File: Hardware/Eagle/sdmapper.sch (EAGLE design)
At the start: 27 parts, among them IC1 AM29F010J, IC2 HM628512ASOP32, IC3 XC95144XL_TQ100, IC4 LM1117-3V3, T1 BC558, T2 BC558

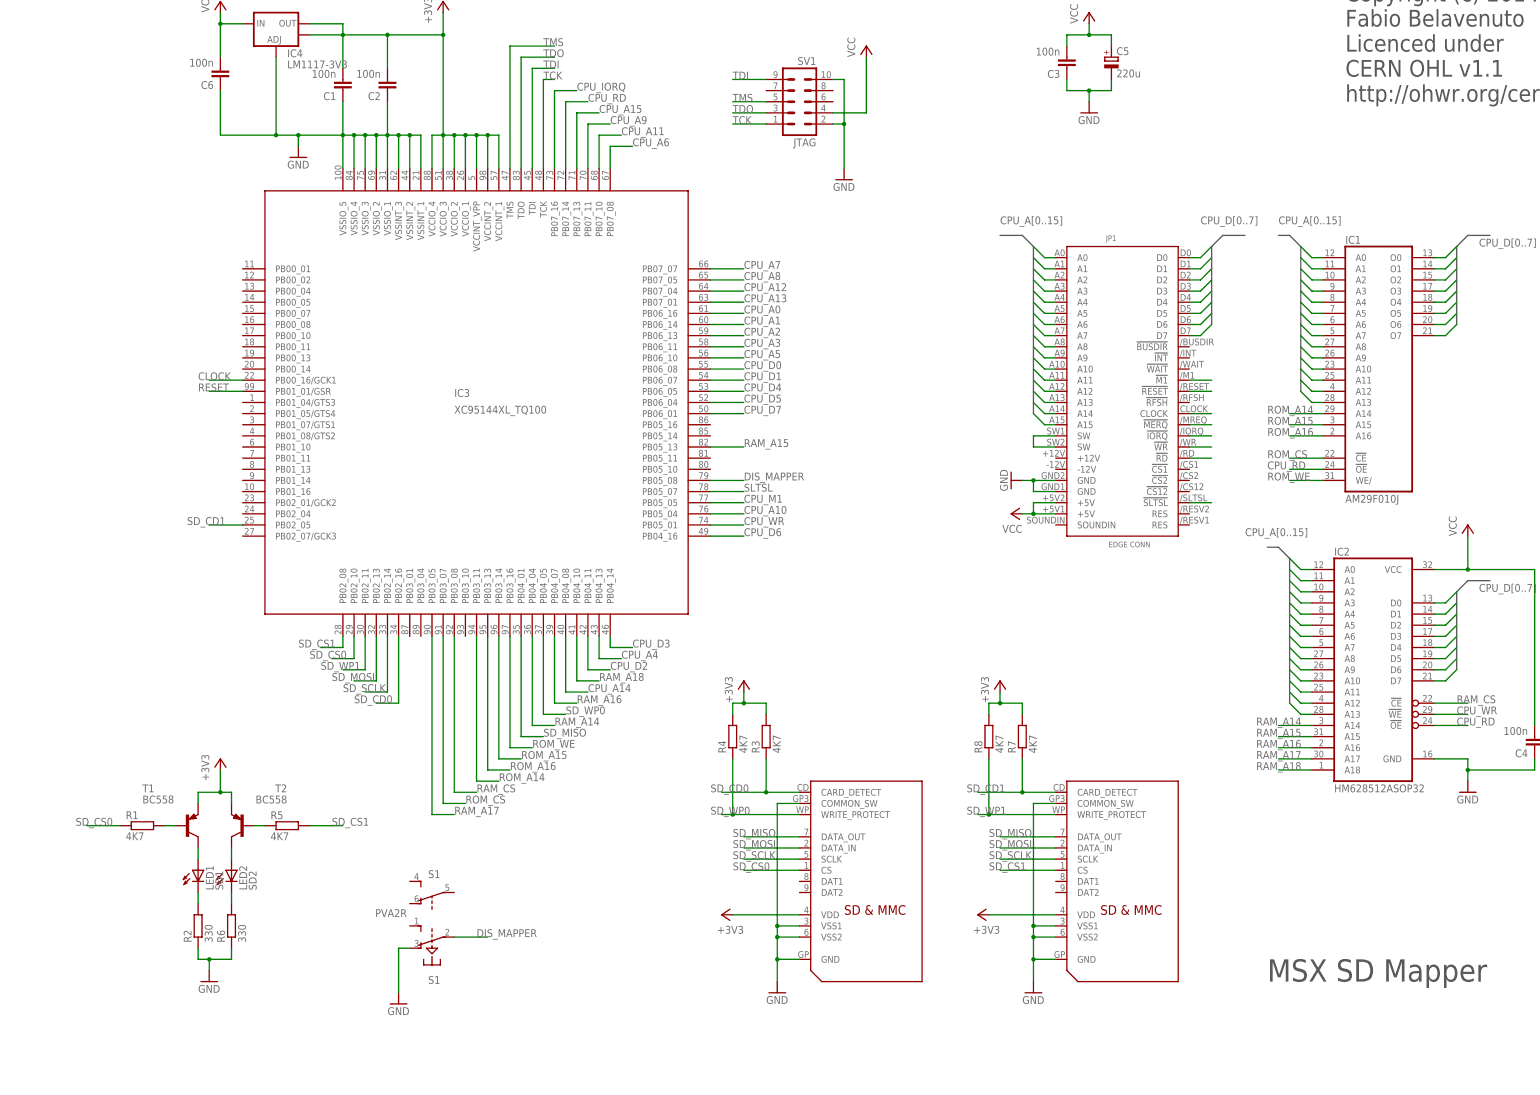
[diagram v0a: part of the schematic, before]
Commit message: Terminado layout da placa Atualizado esquema.pdf Atualizado pinout no projeto do ISE
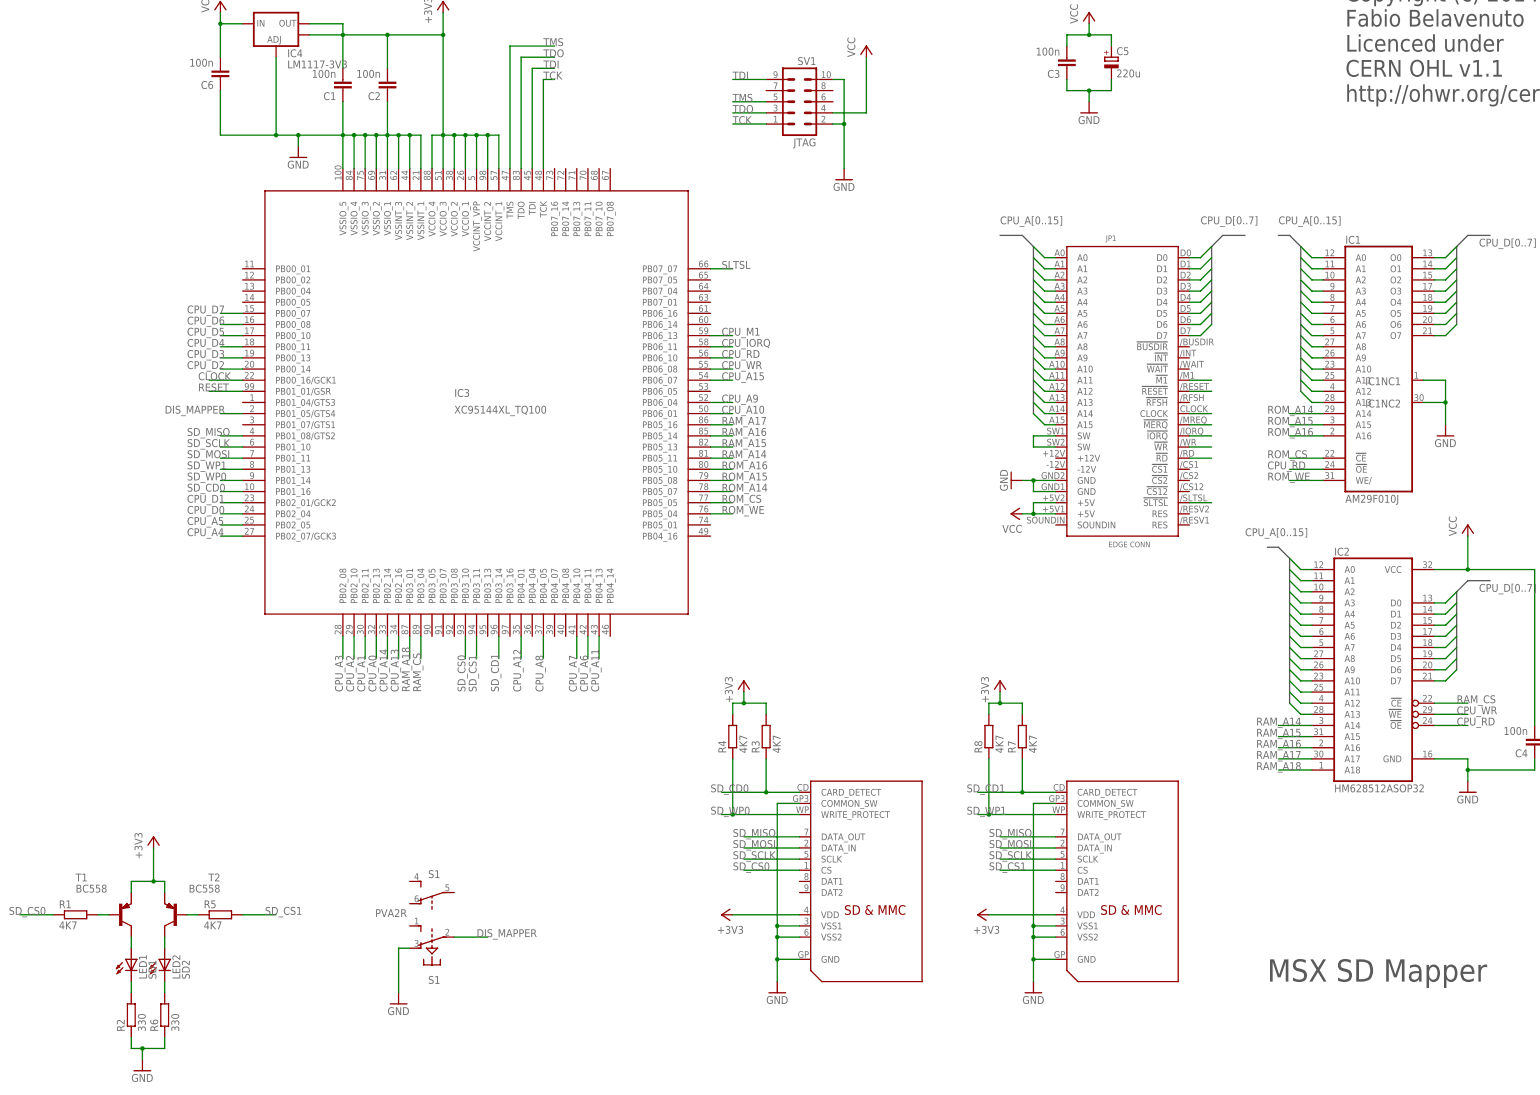
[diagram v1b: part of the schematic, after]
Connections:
- net CPU_A0: now also IC3.PB02_13; no longer IC3.PB06_16
- net CPU_A1: now also IC3.PB02_11; no longer IC3.PB06_14
- net CPU_A10: now also IC3.PB06_01; no longer IC3.PB05_04
- net CPU_A11: now also IC3.PB04_13; no longer IC3.PB07_10
- net CPU_A12: now also IC3.PB04_01; no longer IC3.PB07_04
- net CPU_A13: now also IC3.PB02_16; no longer IC3.PB07_01
- net CPU_A14: now also IC3.PB02_14; no longer IC3.PB04_08
- net CPU_A15: now also IC3.PB06_07; no longer IC3.PB07_13
- net CPU_A2: now also IC3.PB02_10; no longer IC3.PB06_13
- net CPU_A3: now also IC3.PB02_08; no longer IC3.PB06_11
- net CPU_A4: now also IC3.PB02_07/GCK3; no longer IC3.PB04_13
- net CPU_A5: now also IC3.PB02_05; no longer IC3.PB06_10
- net CPU_A6: now also IC3.PB04_11; no longer IC3.PB07_08
- net CPU_A7: now also IC3.PB04_10; no longer IC3.PB07_07
- net CPU_A8: now also IC3.PB04_05; no longer IC3.PB07_05
- net CPU_A9: now also IC3.PB06_04; no longer IC3.PB07_11
- net CPU_D0: now also IC3.PB02_04; no longer IC3.PB06_08
- net CPU_D1: now also IC3.PB02_01/GCK2; no longer IC3.PB06_07
- net CPU_D2: now also IC3.PB00_14; no longer IC3.PB04_11
- net CPU_D3: now also IC3.PB00_13; no longer IC3.PB04_14
- net CPU_D4: now also IC3.PB00_11; no longer IC3.PB06_05
- net CPU_D5: now also IC3.PB00_10; no longer IC3.PB06_04
- net CPU_D6: now also IC3.PB00_08; no longer IC3.PB04_16
- net CPU_D7: now also IC3.PB00_07; no longer IC3.PB06_01
- net CPU_IORQ: now also IC3.PB06_11; no longer IC3.PB07_16
- net CPU_M1: now also IC3.PB06_13; no longer IC3.PB05_05
- net CPU_RD: now also IC3.PB06_10; no longer IC3.PB07_14
- net CPU_WR: now also IC3.PB06_08; no longer IC3.PB05_01
- net DIS_MAPPER: now also IC3.PB01_05/GTS4; no longer IC3.PB05_08
- net GND: now also IC1NC1.NC, IC1NC2.NC
- net RAM_A14: now also IC3.PB05_11; no longer IC3.PB04_04
- net RAM_A16: now also IC3.PB05_14; no longer IC3.PB04_07
- net RAM_A17: now also IC3.PB05_16; no longer IC3.PB03_05
- net RAM_A18: now also IC3.PB03_01; no longer IC3.PB04_10
- net RAM_CS: now also IC3.PB03_04; no longer IC3.PB03_08
- net ROM_A14: now also IC3.PB05_07; no longer IC3.PB03_11
- net ROM_A15: now also IC3.PB05_08; no longer IC3.PB03_14
- net ROM_A16: now also IC3.PB05_10; no longer IC3.PB03_13
- net ROM_CS: now also IC3.PB05_05; no longer IC3.PB03_07
- net ROM_WE: now also IC3.PB05_04; no longer IC3.PB03_16
- net SD_CD0: now also IC3.PB01_16; no longer IC3.PB02_16
- net SD_CD1: now also IC3.PB03_14; no longer IC3.PB02_05
- net SD_CS0: now also IC3.PB03_10; no longer IC3.PB02_10
- net SD_CS1: now also IC3.PB03_11; no longer IC3.PB02_08
- net SD_MISO: now also IC3.PB01_08/GTS2; no longer IC3.PB04_01
- net SD_MOSI: now also IC3.PB01_11; no longer IC3.PB02_13
- net SD_SCLK: now also IC3.PB01_10; no longer IC3.PB02_14
- net SD_WP0: now also IC3.PB01_14; no longer IC3.PB04_05
- net SD_WP1: now also IC3.PB01_13; no longer IC3.PB02_11
- net SLTSL: now also IC3.PB07_07; no longer IC3.PB05_07
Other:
- moved on the sheet: LED1, LED2, R1, R2, R5, R6, T1, T2

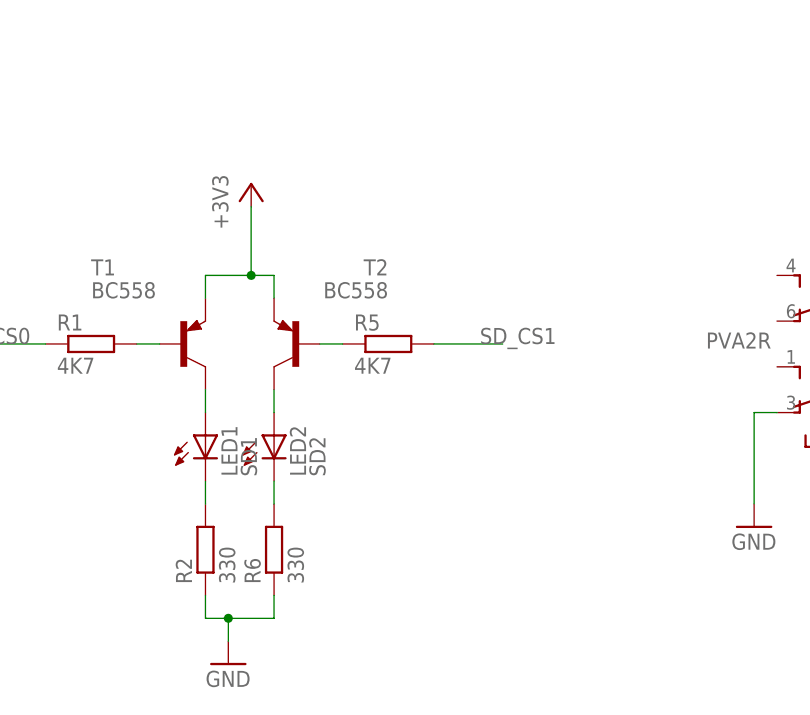
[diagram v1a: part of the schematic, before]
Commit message: Corrigido footprint da SRAM Retirado LEDs comuns e trocado por LED bi-color Layout da placa foi otimizada
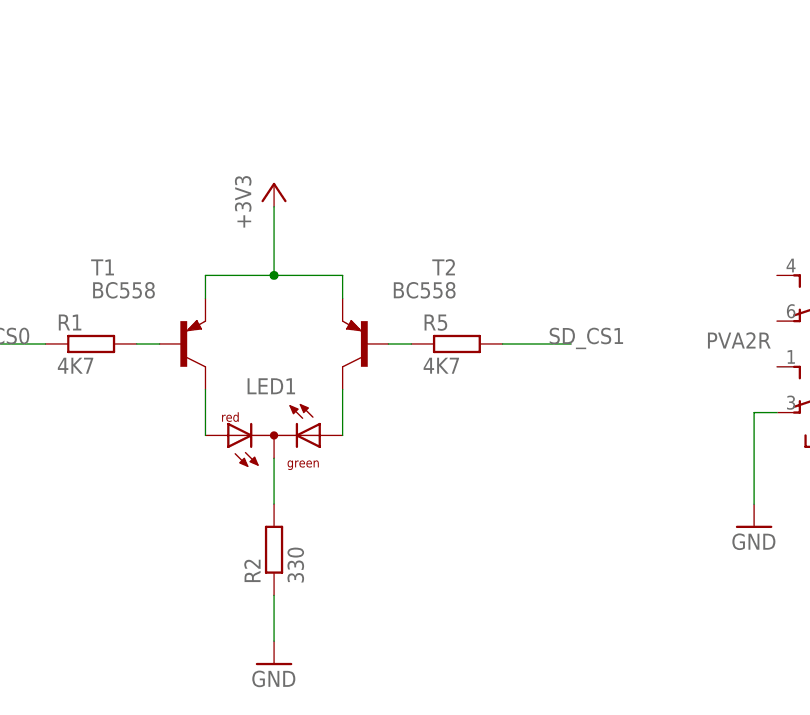
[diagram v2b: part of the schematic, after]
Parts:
- removed LED2: SD2, led:LED3MM
- removed R6: 330, rcl:R-EU_R1206
- LED1: value SD1 -> (none); device led:LED3MM -> led_duoled:DUOLED-RG-C3MM
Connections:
- removed net N$7: LED2.C, R6.2
- net GND: no longer R6.1
- net N$2: now also LED1.AR; no longer LED1.A
- net N$8: now also LED1.AG; no longer LED2.A
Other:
- moved on the sheet: R2, R5, T2

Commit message: Modificado porta SPI no CPLD para trabalhar assincronicamente. Adicionado oscilador de 25MHz na placa. Modificado porta de controle do updater. Estudando desenvolvimento do driver para Symbos
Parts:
- removed LED1: (no value), led_duoled:DUOLED-RG-C3MM
- added C7: 100n, rcl:C-EUC1206
- added D1: Cart1, led:LED3MM
- added D2: Cart2, led:LED3MM
- added R6, R9: 4K7, rcl:R-EU_R1206
- added S2: TL32YO, switch:TL32YO
- C5: device rcl:CPOL-EUE3.5-8 -> rcl:CPOL-EUE2-5
- S1: value PVA2R -> TL32YO; device switch-misc:PVA2R -> switch:TL32YO
- T1, T2: value BC558 -> BC857; device transistor:BC557C-PNP-TO92-EBC -> transistor:BC857C-PNP-SOT23-BEC
- renumbered U$1 to SD1, U$2 to SD2
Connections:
- removed net DIS_MAPPER: IC3.PB01_05/GTS4, S11.P
- removed net N$2: LED1.AR, T1.C
- removed net N$3: LED1.C, R2.2
- new net DIS_MR_MP: IC3.PB01_05/GTS4, R9.1, S1.P
- new net MR_MP: IC3.PB01_04/GTS3, R8.1, S2.P
- new net N$7: D1.C, D2.C, R2.2
- new net N$9: D2.A, T2.C
- new net RAM_A13: IC2.A13, IC3.PB07_11
- new net RAM_WE: IC2.!WE, IC3.PB07_05
- net +3V3: now also C4.2, C6.2, C7.2, R5.2, R6.2, R9.2; no longer C1.2, R3.2
- net CPU_A13: no longer IC2.A13
- net CPU_WR: no longer IC2.!WE
- net GND: now also C7.1, S1.O, S2.O; no longer S11.O
- net N$5: now also R3.1; no longer R5.1
- net N$8: now also D1.A, T1.C; no longer LED1.AG, T2.C
- net SD_CD0: now also R4.1; no longer R3.1
- net SD_CS1: now also R3.2; no longer R5.2
- net SD_WP0: now also R6.1; no longer R4.1
- net SD_WP1: now also R5.1; no longer R8.1
- net VCC: now also C1.2; no longer C4.2, C6.2
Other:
- note added: "Copyright (c) 2014 Fabio Belavenuto Licenced under CERN OHL v1.1 http://ohwr.org/cernohl PCB by Luciano Sturaro"
- note added: "MSX SD Mapper/Megaram"
- note added: "SD1"
- note added: "SD2"
- note removed: "Copyright (c) 2014 Fabio Belavenuto Licenced under CERN OHL v1.1 http://ohwr.org/cernohl"
- note removed: "MSX SD Mapper"
- moved on the sheet: C1, C2, C3, C4, C6, JP1, R1, R2, R3, R4, R5, R8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
